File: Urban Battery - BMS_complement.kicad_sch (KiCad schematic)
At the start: 41 parts, among them J1 BMS IO, J10 E-Stop, J11 Contactor Connector, J12 Thermistor, J13 Thermistor, J14 Thermistor, J2 OLED Header, J3 CAN, J4 CAN, J5 Charge Connector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

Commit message: swapped run and charge labels, changed charge connector, renamed board
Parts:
- J5: footprint Connector_Molex:Molex_Micro-Fit_3.0_43650-0200_1x02_P3.00mm_Horizontal -> Connector_Molex:Molex_Mini-Fit_Jr_5569-02A2_2x01_P4.20mm_Horizontal
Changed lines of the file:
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@@
       (effects (font (size 1.27 1.27)) (justify left))
     )
-    (property "Footprint" "Connector_Molex:Molex_Micro-Fit_3.0_43650-0200_1x02_P3.00mm_Horizontal" (id 2) (at 256.54 58.42 0)
-      (effects (font (size 1.27 1.27)) hide)
-    )
-    (property "Datasheet" "https://www.molex.com/pdm_docs/sd/436500200_sd.pdf" (id 3) (at 256.54 58.42 0)
+    (property "Footprint" "Connector_Molex:Molex_Mini-Fit_Jr_5569-02A2_2x01_P4.20mm_Horizontal" (id 2) (at 256.54 58.42 0)
+      (effects (font (size 1.27 1.27)) hide)
+    )
+    (property "Datasheet" "https://www.molex.com/pdm_docs/ps/PS-5556-001.pdf" (id 3) (at 256.54 58.42 0)
       (effects (font (size 1.27 1.27)) hide)
     )
@@
     )
     (path "/7c8b5bee-9709-44ed-b549-ea2a8e264dfd"
-      (reference "J5") (unit 1) (value "Charge Connector") (footprint "Connector_Molex:Molex_Micro-Fit_3.0_43650-0200_1x02_P3.00mm_Horizontal")
+      (reference "J5") (unit 1) (value "Charge Connector") (footprint "Connector_Molex:Molex_Mini-Fit_Jr_5569-02A2_2x01_P4.20mm_Horizontal")
     )
     (path "/3f5a7f38-1f93-4176-9e51-e94247502669"

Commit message: added downloaded footprint for bms i/o, updated on layout. fixed orientation of charge connector labels
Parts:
- J1: footprint Connector_JST:JST_PHD_S20B-PHDSS_2x10_P2.00mm_Horizontal -> BMS_Custom_Footprints:B20BPADSS1FLFSN
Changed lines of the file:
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@@
     (property "Reference" "J1" (id 0) (at 54.61 46.99 0))
     (property "Value" "BMS IO" (id 1) (at 54.61 49.53 0))
-    (property "Footprint" "Connector_JST:JST_PHD_S20B-PHDSS_2x10_P2.00mm_Horizontal" (id 2) (at 53.34 63.5 0)
-      (effects (font (size 1.27 1.27)) hide)
-    )
-    (property "Datasheet" "https://www.jst-mfg.com/product/pdf/eng/ePHD.pdf" (id 3) (at 53.34 63.5 0)
+    (property "Footprint" "BMS_Custom_Footprints:B20BPADSS1FLFSN" (id 2) (at 53.34 63.5 0)
+      (effects (font (size 1.27 1.27)) hide)
+    )
+    (property "Datasheet" "https://www.jst-mfg.com/product/pdf/eng/ePAD.pdf" (id 3) (at 53.34 63.5 0)
       (effects (font (size 1.27 1.27)) hide)
     )
@@
     )
     (path "/ad19ca46-d501-4728-a593-92fee2c7a96e"
-      (reference "J1") (unit 1) (value "BMS IO") (footprint "Connector_JST:JST_PHD_S20B-PHDSS_2x10_P2.00mm_Horizontal")
+      (reference "J1") (unit 1) (value "BMS IO") (footprint "BMS_Custom_Footprints:B20BPADSS1FLFSN")
     )
     (path "/902b5024-1beb-4d80-b15a-ec47fd783491"

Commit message: updated connector footprints of J6 and J12-J14
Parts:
- J12: footprint TerminalBlock_Phoenix:TerminalBlock_Phoenix_MKDS-1,5-2-5.08_1x02_P5.08mm_Horizontal -> Connector_Molex:Molex_Micro-Fit_3.0_43650-0200_1x02_P3.00mm_Horizontal
- J6: footprint TerminalBlock_Phoenix:TerminalBlock_Phoenix_MKDS-1,5-2-5.08_1x02_P5.08mm_Horizontal -> Connector_Molex:Molex_Mega-Fit_76825-0002_2x01_P5.70mm_Horizontal
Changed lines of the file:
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@@
 			)
 		)
-		(property "Footprint" "TerminalBlock_Phoenix:TerminalBlock_Phoenix_MKDS-1,5-2-5.08_1x02_P5.08mm_Horizontal"
+		(property "Footprint" "Connector_Molex:Molex_Mega-Fit_76825-0002_2x01_P5.70mm_Horizontal"
 			(at 256.54 224.79 0)
 			(effects
@@
 			)
 		)
-		(property "Datasheet" "https://media.digikey.com/pdf/Data%20Sheets/Phoenix%20Contact%20PDFs/Multi-Postion%20PCTerminal%20Blocks.pdf"
+		(property "Datasheet" "https://mm.digikey.com/Volume0/opasdata/d220001/medias/docus/1100/Mega-Fit_Power_Conn.pdf"
 			(at 256.54 224.79 0)
 			(effects
@@
 			)
 		)
-		(property "Footprint" "TerminalBlock_Phoenix:TerminalBlock_Phoenix_MKDS-1,5-2-5.08_1x02_P5.08mm_Horizontal"
+		(property "Footprint" "Connector_Molex:Molex_Micro-Fit_3.0_43650-0200_1x02_P3.00mm_Horizontal"
 			(at 261.62 185.42 0)
 			(effects
@@
 			)
 		)
-		(property "Datasheet" "https://www.digikey.ca/en/products/detail/phoenix-contact/1729128/260615?utm_adgroup=Connectors%2C%20Interconnects&utm_source=google&utm_medium=cpc&utm_campaign=Shopping_Supplier_Phoenix%20Contact_0277_Co-op&utm_term=&productid=260615&gclid=CjwKCAiAhqCdBhB0EiwAH8M_GunPOPKCx2ICSjHcvsaLY6vUI2QZJvTEruKzXstBsW3mdooGzr9-MRoCGRIQAvD_BwE"
+		(property "Datasheet" "https://www.molex.com/content/dam/molex/molex-dot-com/products/automated/en-us/salesdrawingpdf/436/43650/436500200_sd.pdf?inline"
 			(at 261.62 185.42 0)
 			(effects

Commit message: updated J13, J14 footprints and datasheets to match J12
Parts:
- J13, J14: footprint TerminalBlock_Phoenix:TerminalBlock_Phoenix_MKDS-1,5-2-5.08_1x02_P5.08mm_Horizontal -> Connector_Molex:Molex_Micro-Fit_3.0_43650-0200_1x02_P3.00mm_Horizontal
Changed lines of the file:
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@@
 		)
 		(property "Intersheetrefs" "${INTERSHEET_REFS}"
-			(at 247.8374 194.2306 0)
+			(at 247.2654 194.31 0)
 			(effects
 				(font
@@
 			)
 		)
-		(property "Footprint" "TerminalBlock_Phoenix:TerminalBlock_Phoenix_MKDS-1,5-2-5.08_1x02_P5.08mm_Horizontal"
+		(property "Footprint" "Connector_Molex:Molex_Micro-Fit_3.0_43650-0200_1x02_P3.00mm_Horizontal"
 			(at 261.62 191.77 0)
 			(effects
@@
 			)
 		)
-		(property "Datasheet" "https://www.digikey.ca/en/products/detail/phoenix-contact/1729128/260615?utm_adgroup=Connectors%2C%20Interconnects&utm_source=google&utm_medium=cpc&utm_campaign=Shopping_Supplier_Phoenix%20Contact_0277_Co-op&utm_term=&productid=260615&gclid=CjwKCAiAhqCdBhB0EiwAH8M_GunPOPKCx2ICSjHcvsaLY6vUI2QZJvTEruKzXstBsW3mdooGzr9-MRoCGRIQAvD_BwE"
+		(property "Datasheet" "https://www.molex.com/content/dam/molex/molex-dot-com/products/automated/en-us/salesdrawingpdf/436/43650/436500200_sd.pdf?inline"
 			(at 261.62 191.77 0)
 			(effects
@@
 			)
 		)
-		(property "Footprint" "TerminalBlock_Phoenix:TerminalBlock_Phoenix_MKDS-1,5-2-5.08_1x02_P5.08mm_Horizontal"
+		(property "Footprint" "Connector_Molex:Molex_Micro-Fit_3.0_43650-0200_1x02_P3.00mm_Horizontal"
 			(at 261.62 198.12 0)
 			(effects
@@
 			)
 		)
-		(property "Datasheet" "https://www.digikey.ca/en/products/detail/phoenix-contact/1729128/260615?utm_adgroup=Connectors%2C%20Interconnects&utm_source=google&utm_medium=cpc&utm_campaign=Shopping_Supplier_Phoenix%20Contact_0277_Co-op&utm_term=&productid=260615&gclid=CjwKCAiAhqCdBhB0EiwAH8M_GunPOPKCx2ICSjHcvsaLY6vUI2QZJvTEruKzXstBsW3mdooGzr9-MRoCGRIQAvD_BwE"
+		(property "Datasheet" "https://www.molex.com/content/dam/molex/molex-dot-com/products/automated/en-us/salesdrawingpdf/436/43650/436500200_sd.pdf?inline"
 			(at 261.62 198.12 0)
 			(effects

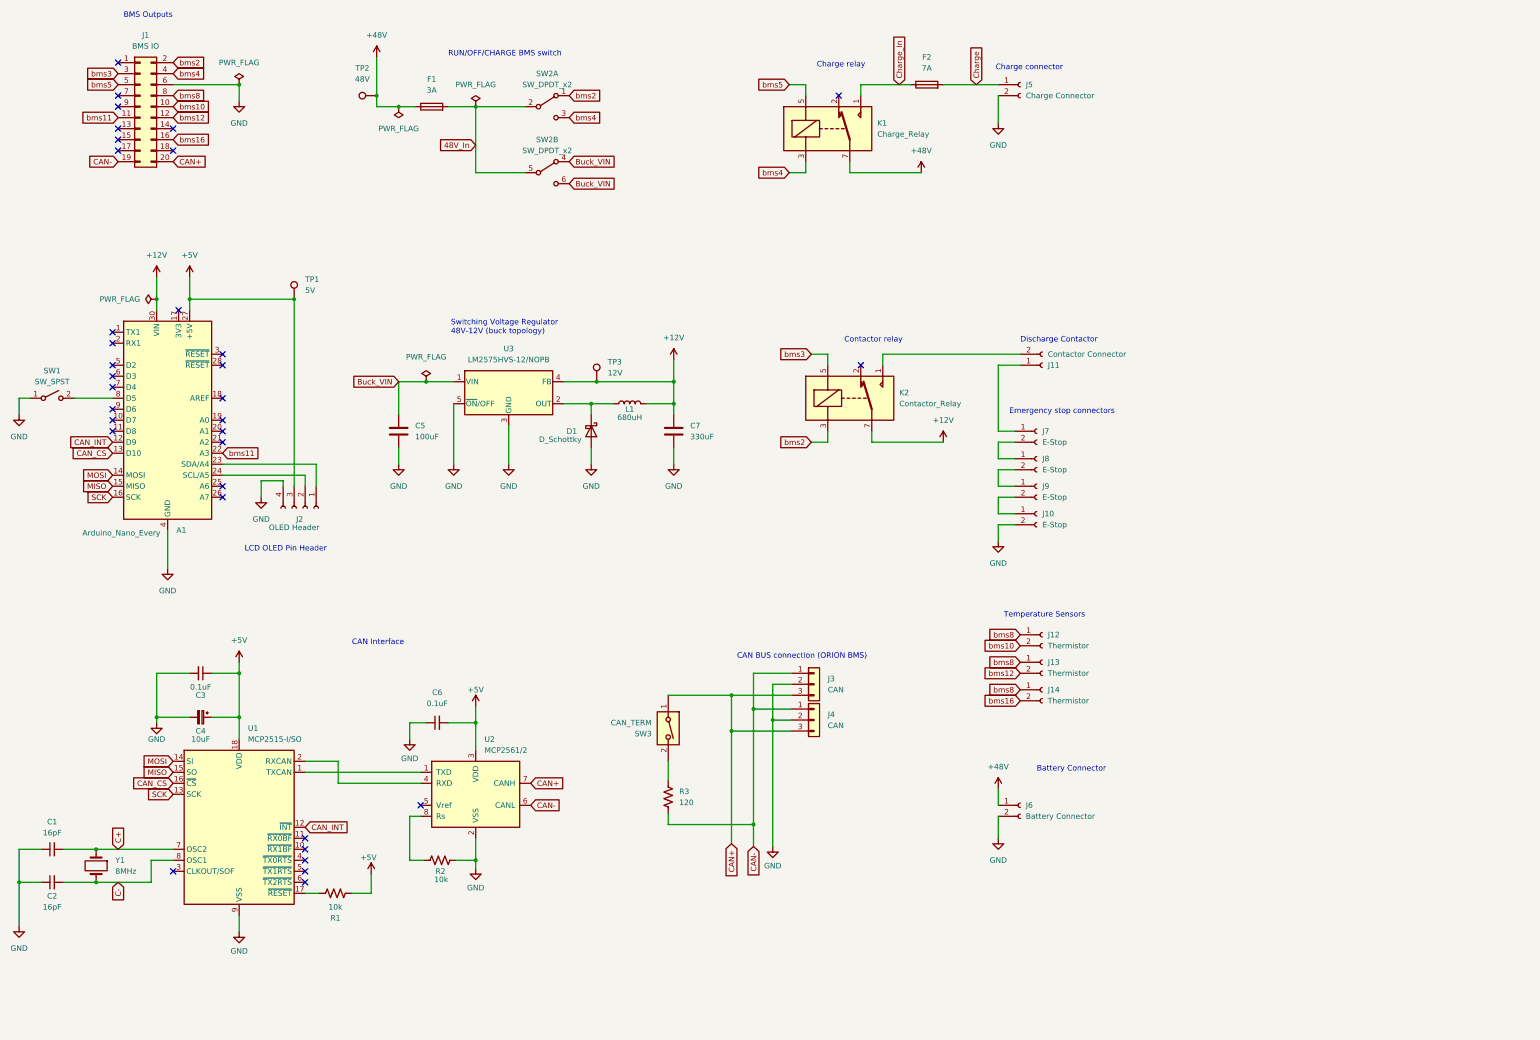
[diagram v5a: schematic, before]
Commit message: Added new CAN and killswitch connector DigiKey symbols
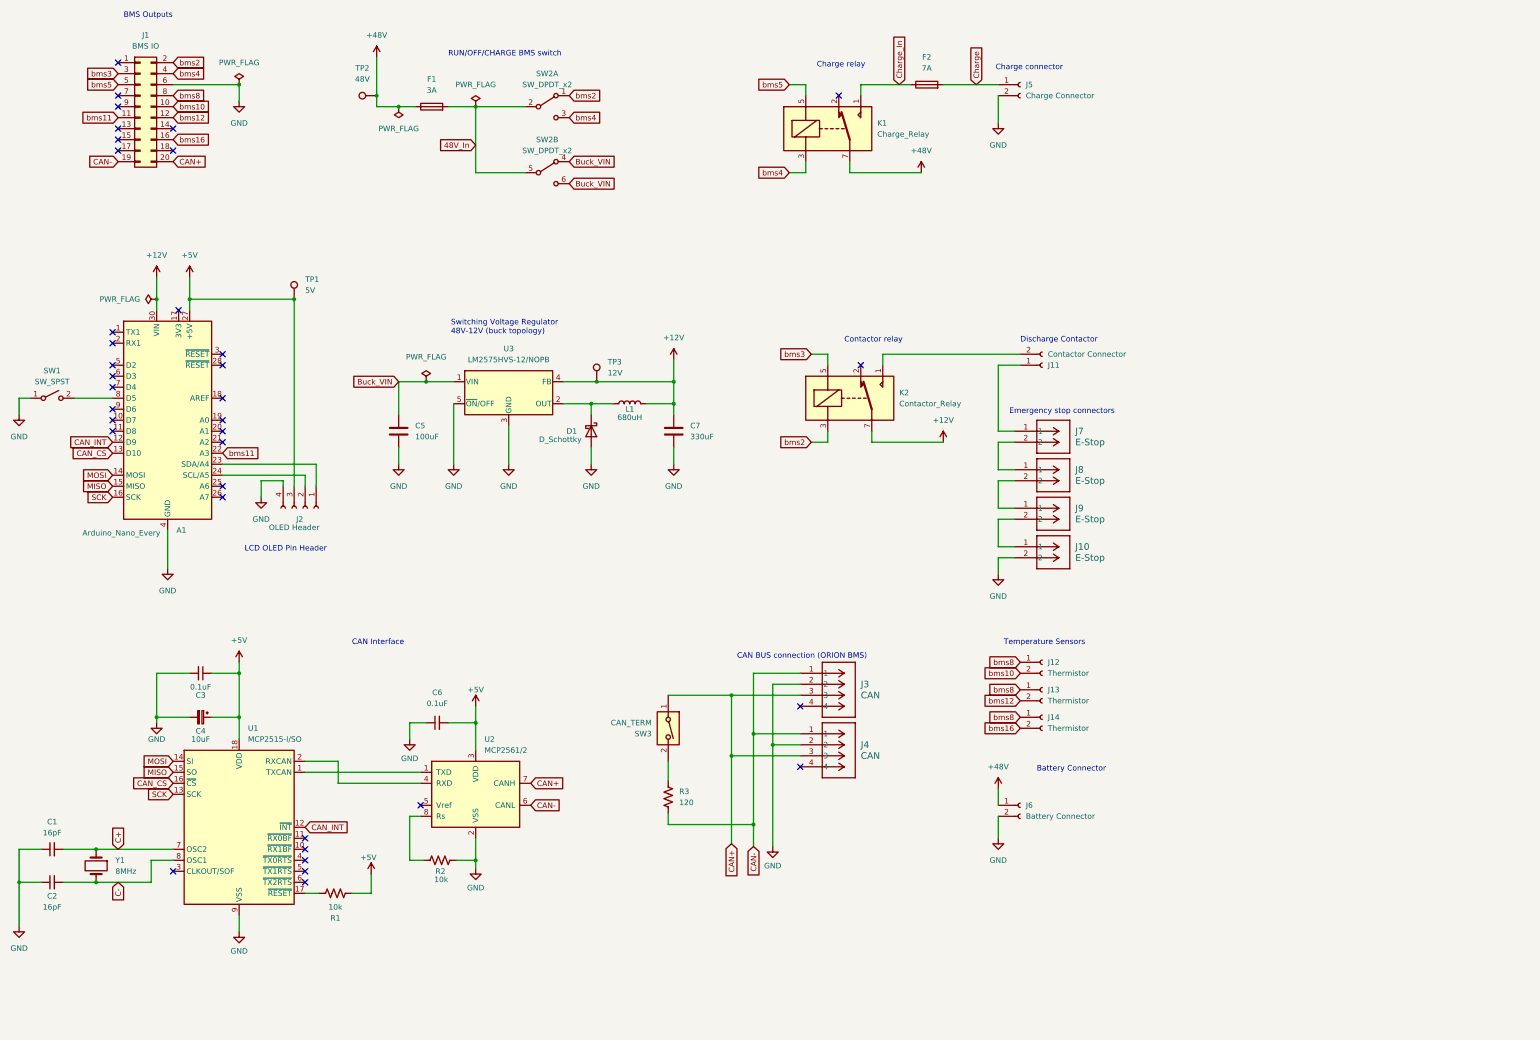
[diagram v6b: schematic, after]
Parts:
- removed J10, J7, J8, J9: E-Stop, Connector_Molex:Molex_Micro-Fit_3.0_43650-0200_1x02_P3.00mm_Horizontal, symbol Connector:Conn_01x02_Female
- removed J3, J4: CAN, BMS_Custom_Footprints:molex-sl-1x03-horizontal, symbol Connector_Generic:Conn_01x03
- added J10, J7, J8, J9: E-Stop, CONN_5569-02A_MOL, symbol molex_Minifit_Jr_5569_killswitch_conn:39300020
- added J3, J4: CAN, CONN_5569-04A_MOL, symbol molex_Minifit_Jr_5569_CAN_conn:39301040
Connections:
- net CAN+: now also J3.3, J4.3
- net CAN-: now also J3.1, J4.1
- net GND: now also J10.2, J3.2, J4.2
- net at J11.1 (Pin_1): now also J7.1
- new net: J7.2, J8.1
- new net: J8.2, J9.1
- new net: J10.1, J9.2
- no-connect marks 34 -> 36
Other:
- moved on the sheet: J12, J13, J14

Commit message: Added test pin headers for BMS output, killswitches, Arduino and Buck converter
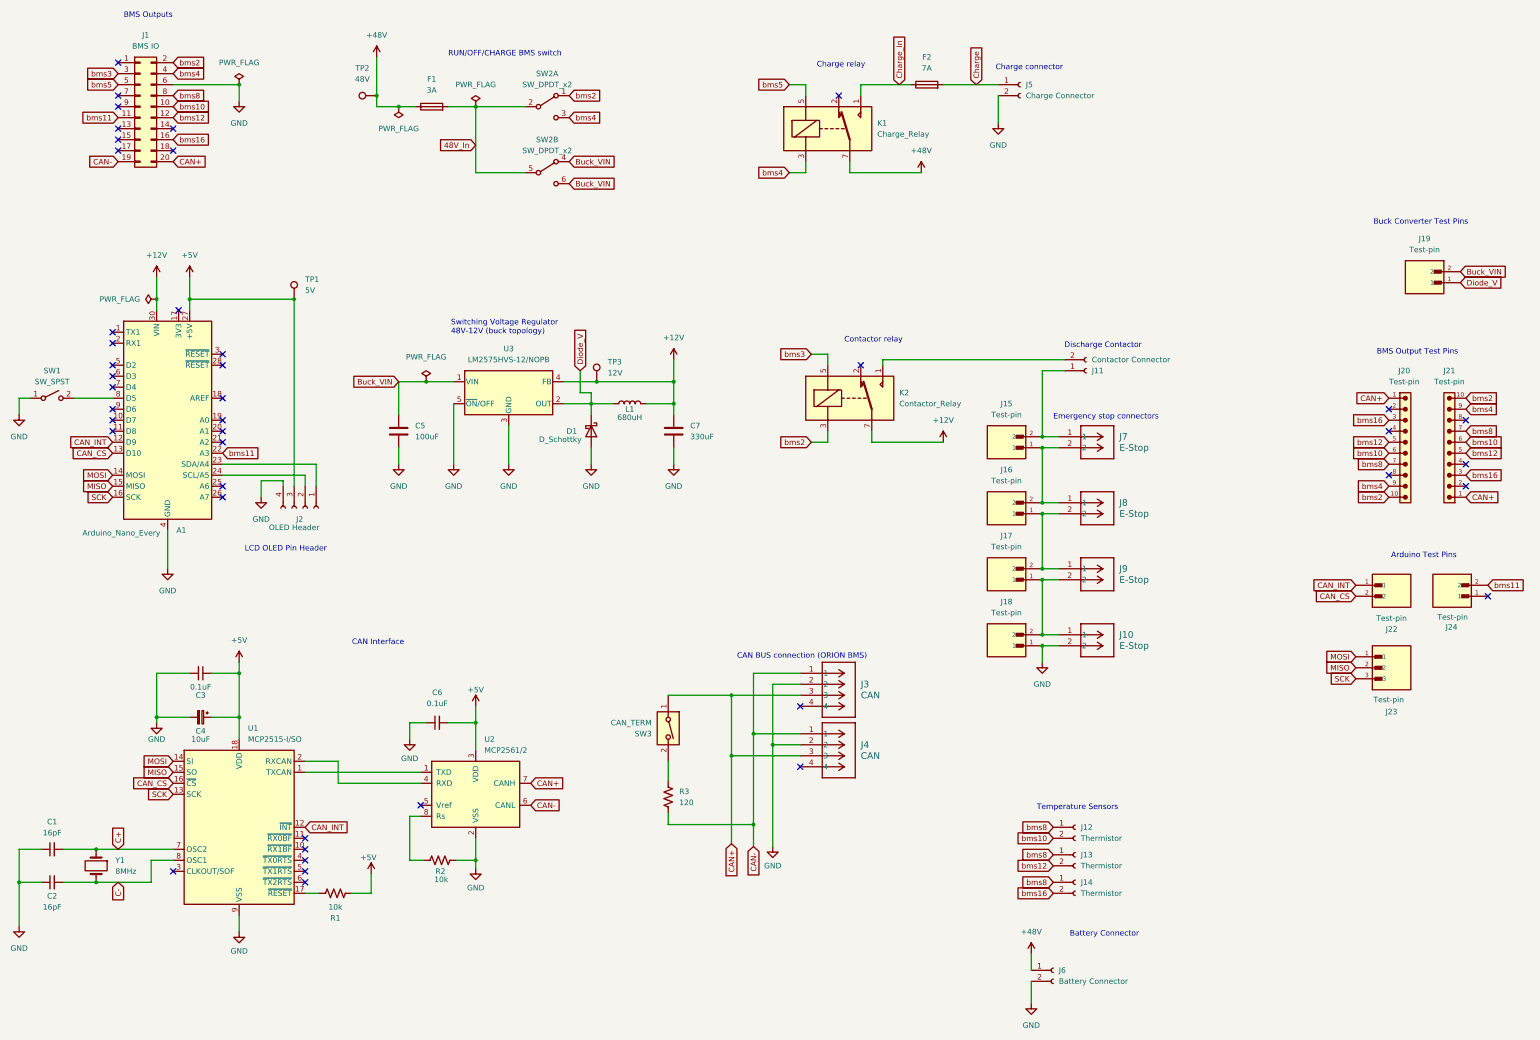
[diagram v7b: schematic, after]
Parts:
- added J15, J16, J17, J18, J19, J22, J24: Test-pin, M20-9990246:HARWIN_M20-9990246, symbol killswitch_test_pin_headers:M20-9990246
- added J20, J21: Test-pin, 6130XX11121_61301011121:61301011121, symbol BMS_out_10_pin:6130XX11121_61301011121
- added J23: Test-pin, 61300311121:WURTH_61300311121, symbol Arduino_3_pin_61300311121:61300311121
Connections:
- net Buck_VIN: now also J19.2
- net CAN+: now also J20.1, J21.1
- net CAN_CS: now also J22.2
- net CAN_INT: now also J22.1
- net GND: now also J18.1
- net MISO: now also J23.2
- net MOSI: now also J23.1
- net SCK: now also J23.3
- net bms10: now also J20.6, J21.6
- net bms11: now also J24.2
- net bms12: now also J20.5, J21.5
- net bms16: now also J20.3, J21.3
- net bms2: now also J20.10, J21.10
- net bms4: now also J20.9, J21.9
- net bms8: now also J20.7, J21.7
- net Diode_V: now reaches D1.1 (K), L1.1, U3.2 (OUT)
- net Diode_V: now also J19.1
- net at J7.2, J8.1: now also J15.1, J16.2
- net at J8.2, J9.1: now also J16.1, J17.2
- net at J10.1, J9.2: now also J17.1, J18.2
- net at J11.1 (Pin_1), J7.1: now also J15.2
- no-connect marks 36 -> 43
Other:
- note added: "Arduino Test Pins"
- note added: "BMS Output Test Pins"
- note added: "Buck Converter Test Pins"
- moved on the sheet: J10, J11, J12, J13, J14, J6, J7, J8, J9
